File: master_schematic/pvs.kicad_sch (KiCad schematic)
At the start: 12 parts, among them Q1 IRLZ34NPBF, Q2 IRLZ34NPBF, Q3 IRLZ34NPBF, Q4 IRLZ34NPBF

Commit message: modified for PCB development
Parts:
- added D5, D6, D7, D8, D9: FERD20H100STS, symbol Device:D
- added L5, L6, L7, L8, L9: Solenoid, symbol Device:L
- added Q5, Q6, Q7, Q8, Q9: IRLZ34NPBF, IRLZ34NPBF:TO-220AB_INF, symbol Transistor_FET:IRLZ34N
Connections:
- net +12V: now also D5.1 (K), D6.1 (K), D7.1 (K), D8.1 (K), D9.1 (K), L5.1, L6.1, L7.1, L8.1, L9.1
- net GND: now also Q5.3 (S), Q6.3 (S), Q7.3 (S), Q8.3 (S), Q9.3 (S)
- new net: D7.2 (A), L7.2, Q7.2 (D)
- new net: D5.2 (A), L5.2, Q5.2 (D)
- new net: D9.2 (A), L9.2, Q9.2 (D)
- new net: D6.2 (A), L6.2, Q6.2 (D)
- new net: D8.2 (A), L8.2, Q8.2 (D)
- new net BV1-O: Q9.1 (G)
- new net BV1-P: Q7.1 (G)
- new net BV1-T: Q8.1 (G)
- new net MBV1-I-1: Q5.1 (G)
- new net MBV1-I-2: Q6.1 (G)
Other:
- note added: "Bleed valves"
- note added: "Motorized Ball Valve"
- note added: "Power Valves"
- note removed: "Power Valve"
- moved on the sheet: D1, D2, D3, D4, L1, L2, L3, L4, Q1, Q2, Q3, Q4

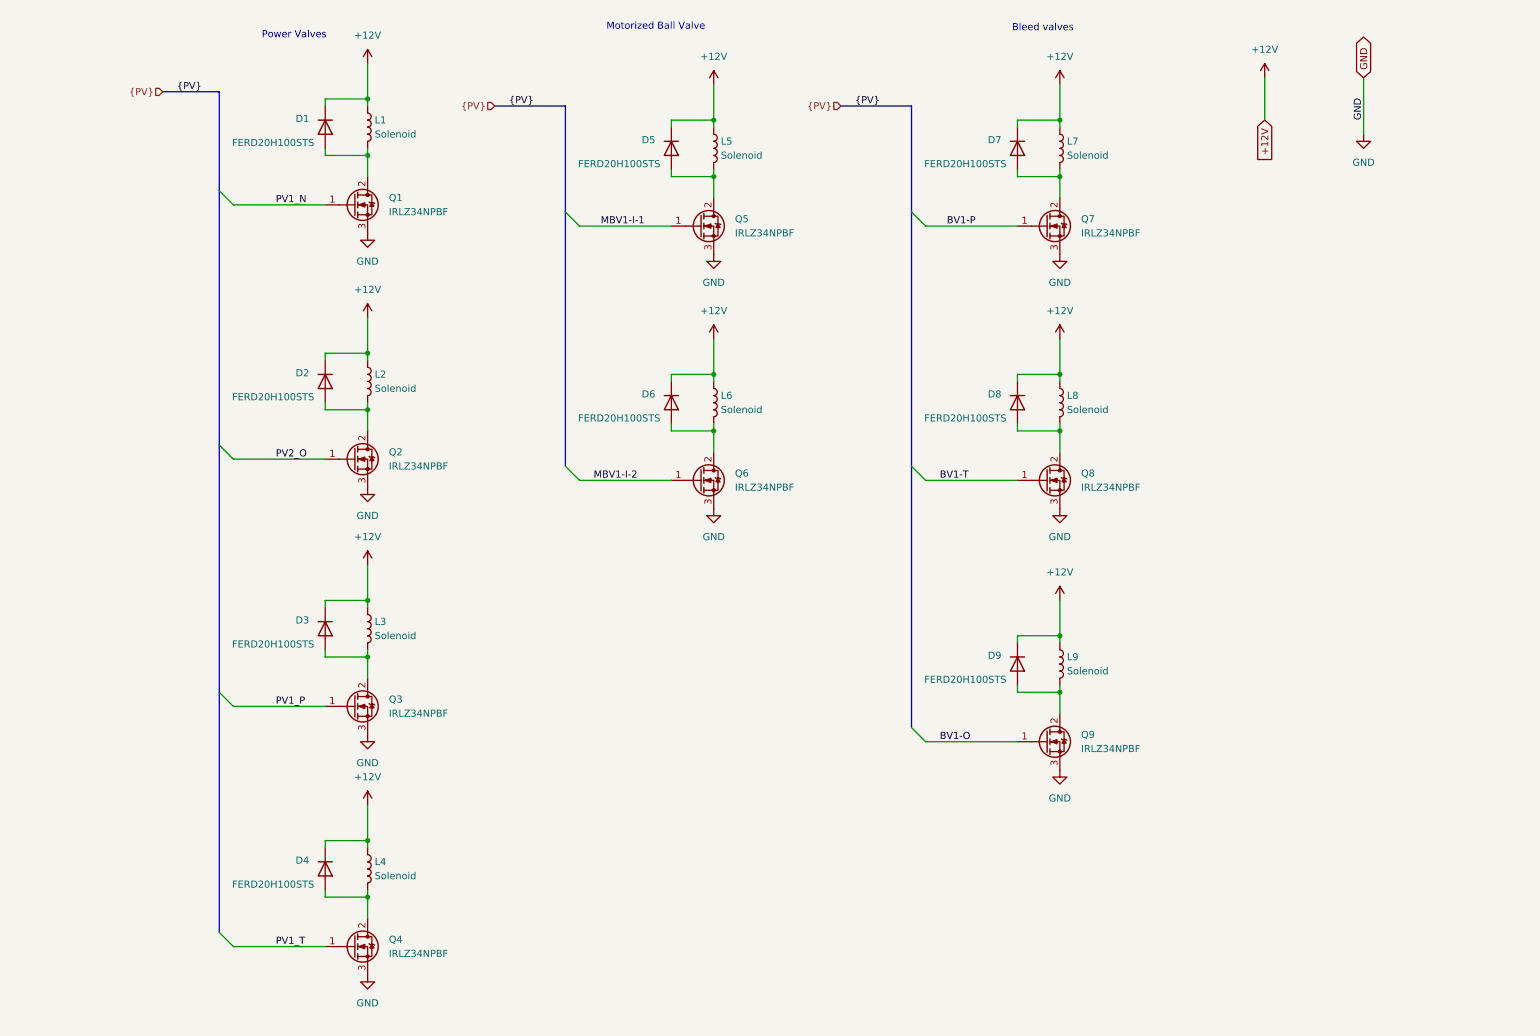
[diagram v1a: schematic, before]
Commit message: updated with part info
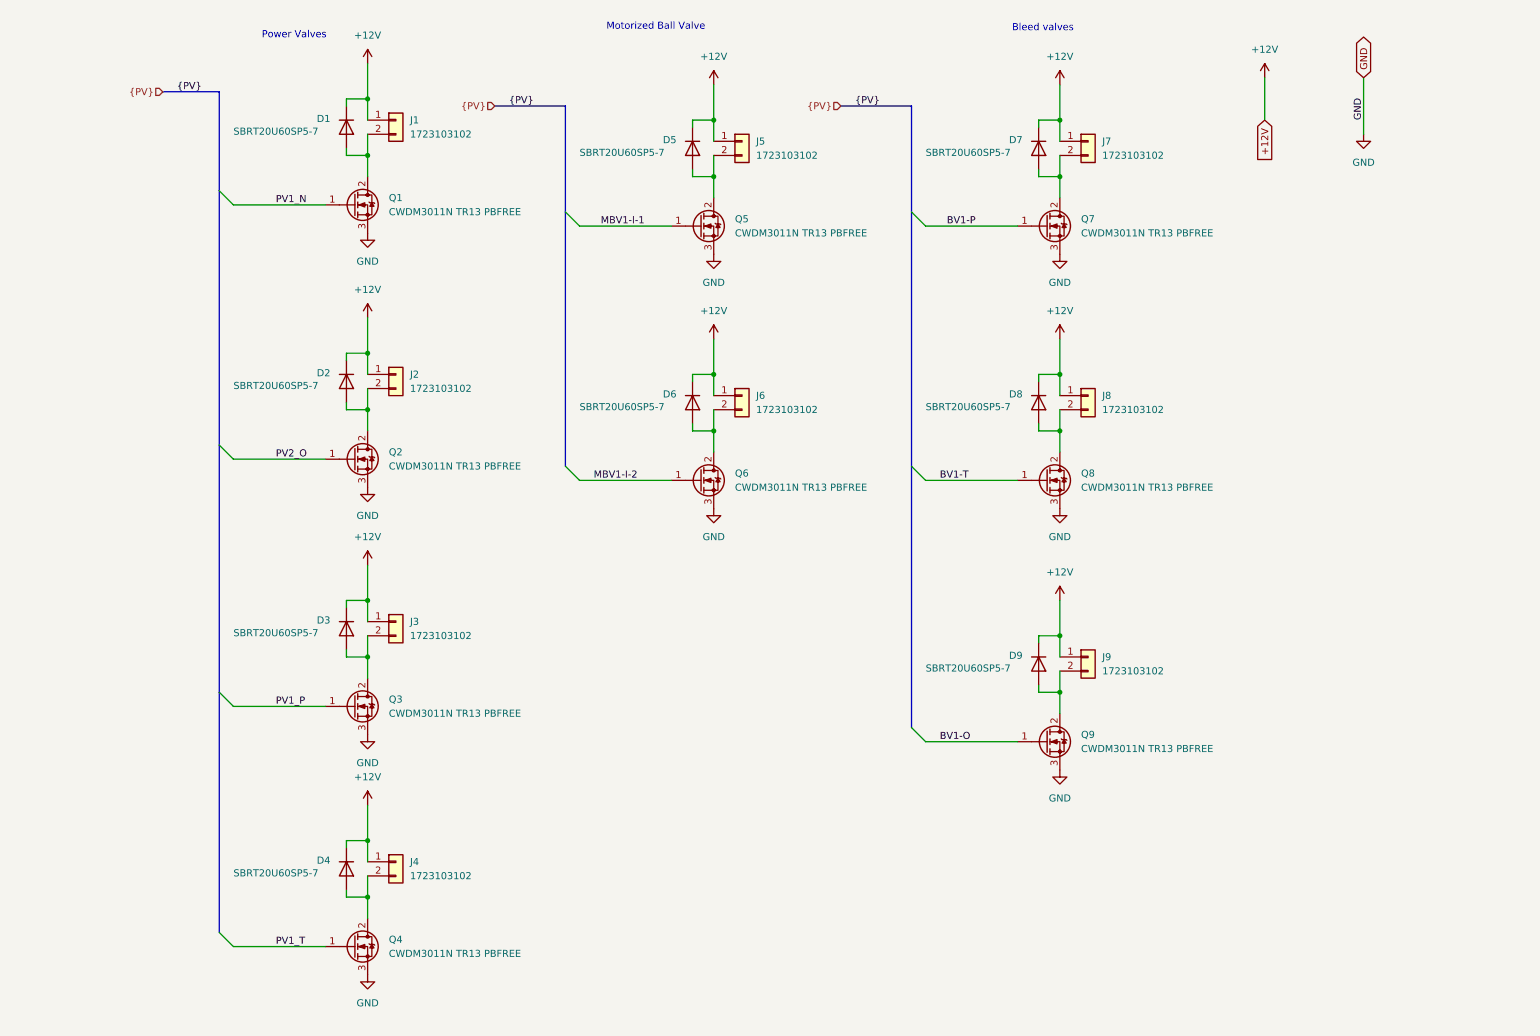
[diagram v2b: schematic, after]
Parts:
- removed L1, L2, L3, L4, L5, L6, L7, L8, L9: Solenoid, symbol Device:L
- added J1, J2, J3, J4, J5, J6, J7, J8, J9: 1723103102, hb_footprint_lib:CONN02_1723103102_MOL, symbol Connector_Generic:Conn_01x02
- D1, D2, D3, D4, D5, D6, D7, D8, D9: value FERD20H100STS -> SBRT20U60SP5-7; footprint (none) -> hb_footprint_lib:POWERDI5_DIO; Cost @ Qty (none) -> 0.78; Manufacturer (none) -> Diodes Incorporated; Manufacturer Part # (none) -> SBRT20U60SP5-7; Supplier (none) -> Digikey; Supplier Part # (none) -> SBRT20U60SP5-7DICT-ND; Unit Cost (none) -> 0.78
- Q1, Q2, Q3, Q4, Q5, Q6, Q7, Q8, Q9: value IRLZ34NPBF -> CWDM3011N TR13 PBFREE; footprint IRLZ34NPBF:TO-220AB_INF -> Package_SO:SOIC-8_3.9x4.9mm_P1.27mm; Cost @ Qty (none) -> 1.09; Manufacturer (none) -> Central Semiconductor Corp; Manufacturer Part # (none) -> CWDM3011N TR13 PBFREE; Supplier (none) -> Digikey; Supplier Part # (none) -> 1514-CWDM3011NTR13PBFREECT-ND; Unit Cost (none) -> 1.09
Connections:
- net +12V: now also J1.1 (Pin_1), J2.1 (Pin_1), J3.1 (Pin_1), J4.1 (Pin_1), J5.1 (Pin_1), J6.1 (Pin_1), J7.1 (Pin_1), J8.1 (Pin_1), J9.1 (Pin_1)
- net at D1.2 (A), Q1.2 (D): now also J1.2 (Pin_2)
- net at D7.2 (A), Q7.2 (D): now also J7.2 (Pin_2)
- net at D4.2 (A), Q4.2 (D): now also J4.2 (Pin_2)
- net at D5.2 (A), Q5.2 (D): now also J5.2 (Pin_2)
- net at D3.2 (A), Q3.2 (D): now also J3.2 (Pin_2)
- net at D2.2 (A), Q2.2 (D): now also J2.2 (Pin_2)
- net at D9.2 (A), Q9.2 (D): now also J9.2 (Pin_2)
- net at D6.2 (A), Q6.2 (D): now also J6.2 (Pin_2)
- net at D8.2 (A), Q8.2 (D): now also J8.2 (Pin_2)
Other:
- moved on the sheet: D1

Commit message: fixed errors on schematic
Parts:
- renumbered J1 to J11, J2 to J12, J3 to J13, J4 to J14, J5 to J15, J6 to J16, J7 to J17, J8 to J18, J9 to J19
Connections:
- net PV2_O renamed PV1_O

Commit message: added decoupling capacitors, fixed voltage values for TTs and load cells to +3V3
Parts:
- added C1, C10, C2, C3, C4, C5, C6, C7, C8, C9: 0.1u, Capacitor_SMD:C_0805_2012Metric, symbol Device:C
- added D7: SBRT20U60SP5-7, hb_footprint_lib:POWERDI5_DIO, symbol Device:D
- added J17: 1723103102, hb_footprint_lib:CONN02_1723103102_MOL, symbol Connector_Generic:Conn_01x02
- added Q7: CWDM3011N TR13 PBFREE, Package_SO:SOIC-8_3.9x4.9mm_P1.27mm, symbol Transistor_FET:IRLZ34N
- renumbered D9 to D10, D7 to D8, D8 to D9, J17 to J18, J18 to J19, J19 to J20, Q9 to Q10, Q7 to Q8, Q8 to Q9
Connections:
- net +12V: now also D7.1 (K), J17.1 (Pin_1)
- net BV1-O: now also C10.1
- net BV1-P: now also C8.1
- net BV1-T: now also C9.1
- net GND: now also C1.2, C10.2, C2.2, C3.2, C4.2, C5.2, C6.2, C7.2, C8.2, C9.2, Q7.3 (S)
- net MBV1-I-1: now also C5.1
- net MBV1-I-2: now also C6.1
- net PV1_N: now also C1.1
- net PV1_O: now also C2.1
- net PV1_P: now also C3.1
- net PV1_T: now also C4.1
- new net: D7.2 (A), J17.2 (Pin_2), Q7.2 (D)
- new net PV2_O: C7.1, Q7.1 (G)

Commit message: finding parts
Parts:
- C1, C10, C2, C3, C4, C5, C6, C7, C8, C9: Cost @ Qty (none) -> 0.026; Manufacturer (none) -> KYOCERA AVX; Manufacturer Part # (none) -> KGM21NR71H104KT; Supplier (none) -> Digikey; Supplier Part # (none) -> 478-KGM21NR71H104KTCT-ND; Unit Cost (none) -> 0.08

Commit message: edits after bom
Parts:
- added J54, J55, J56, J57, J58, J59, J60, J61, J62, J63: 1723103102, hb_footprint_lib:CONN02_1723103102_MOL, symbol Connector_Generic:Conn_01x02
- added J64, J65, J66, J67, J68, J69, J70, J71, J72, J73, J74, J75, J76, J77, J78, J79, J80, J81, J82, J83: 1722563102, symbol Connector_Generic:Conn_01x02
- J11, J12, J13, J14, J15, J16, J17, J18, J19, J20: Cost @ Qty 0.85 -> 0.725
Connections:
- no-connect marks 0 -> 60
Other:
- note added: "Female connectors (same as on board connector)"
- note added: "Male connectors (to make connection with board)"
- moved on the sheet: C1, C10, C2, C3, C4, C5, C6, C7, C8, C9, D1, D10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
